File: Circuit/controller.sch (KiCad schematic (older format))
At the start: 13 parts, among them SW2 ROTARY_ENCODER_SWITCH, SW4 A, SW6 B, U4 JOYSTICK_W_BUTTON

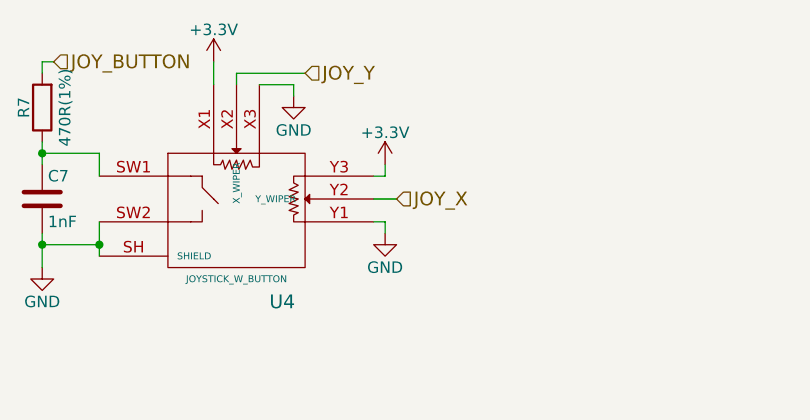
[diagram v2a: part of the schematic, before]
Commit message: Just caught I/O error on controller sch. XY reversed.
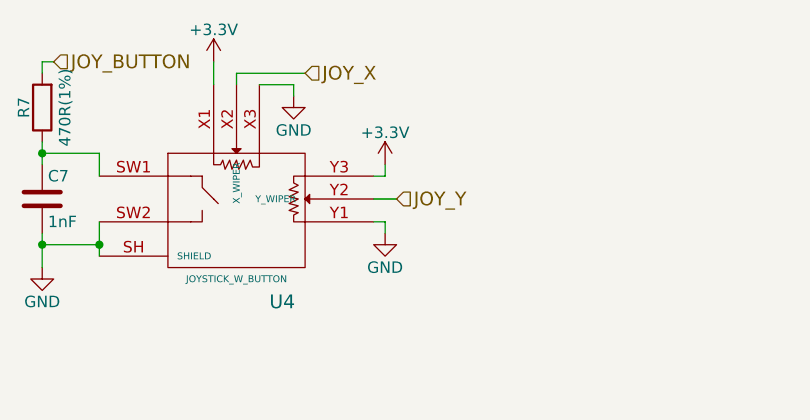
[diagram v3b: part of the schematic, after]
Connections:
- net JOY_X: now also U4.X2 (X_WIPER); no longer U4.Y2 (Y_WIPER)
- net JOY_Y: now also U4.Y2 (Y_WIPER); no longer U4.X2 (X_WIPER)
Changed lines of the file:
@@
 Text HLabel 1000 850  2    60   Input ~ 0
 JOY_BUTTON
+Text HLabel 2100 900  2    60   Input ~ 0
+JOY_X
 Text HLabel 2500 1450 2    60   Input ~ 0
-JOY_X
-Text HLabel 2100 900  2    60   Input ~ 0
 JOY_Y
 Wire Wire Line

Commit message: Modifications for BOM generation & documentation. LAST COMMIT WAS v0.1 PROTOTYPE.
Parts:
- SW2, SW4, SW6, U4: Non-Digikey (none) -> 1
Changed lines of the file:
@@
 F 2 "freetronics_footprints:JOYSTICK_W_BUTTON" H 1800 1450 60  0001 C CNN
 F 3 "" H 1900 850 60  0000 C CNN
+F 4 "1" H 1800 1450 60  0001 C CNN "Non-Digikey"
 	1    1800 1450
 	1    0    0    -1
@@
 F 2 "freetronics_footprints:SW_PUSHBUTTON_PTH" H 4950 1300 50  0001 C CNN
 F 3 "" H 4950 1300 50  0000 C CNN
+F 4 "1" H 4950 1300 60  0001 C CNN "Non-Digikey"
 	1    4950 1300
 	0    -1   -1   0
@@
 F 2 "freetronics_footprints:SW_PUSHBUTTON_PTH" H 4950 2350 50  0001 C CNN
 F 3 "" H 4950 2350 50  0000 C CNN
+F 4 "1" H 4950 2350 60  0001 C CNN "Non-Digikey"
 	1    4950 2350
 	0    -1   -1   0
@@
 F 2 "libs:EC11" H 2100 3910 50  0001 C CNN
 F 3 "" H 2200 4010 50  0001 C CNN
+F 4 "1" H 2200 3750 60  0001 C CNN "Non-Digikey"
 	1    2200 3750
 	1    0    0    -1

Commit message: pcb footprint updates
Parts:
- SW2: value ROTARY_ENCODER_SWITCH -> ROTARY_ENCODER
- U4: value JOYSTICK_W_BUTTON -> JOYSTICK
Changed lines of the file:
@@
 P 1800 1450
 F 0 "U4" H 2000 1000 60  0000 C CNN
-F 1 "JOYSTICK_W_BUTTON" H 1800 1100 30  0000 C CNN
+F 1 "JOYSTICK" H 1800 1100 30  0000 C CNN
 F 2 "freetronics_footprints:JOYSTICK_W_BUTTON" H 1800 1450 60  0001 C CNN
 F 3 "" H 1900 850 60  0000 C CNN
@@
 $EndComp
 $Comp
-L GND #PWR046
+L GND #PWR047
 U 1 1 58137F56
 P 950 1750
-F 0 "#PWR046" H 950 1500 50  0001 C CNN
+F 0 "#PWR047" H 950 1500 50  0001 C CNN
 F 1 "GND" H 950 1600 50  0000 C CNN
 F 2 "" H 950 1750 50  0000 C CNN
@@
 $EndComp
 $Comp
-L +3.3V #PWR047
+L +3.3V #PWR048
 U 1 1 58137F70
 P 1700 850
-F 0 "#PWR047" H 1700 700 50  0001 C CNN
+F 0 "#PWR048" H 1700 700 50  0001 C CNN
 F 1 "+3.3V" H 1700 990 50  0000 C CNN
 F 2 "" H 1700 850 50  0000 C CNN
@@
 	2050 950  2050 1000
 $Comp
-L GND #PWR048
+L GND #PWR049
 U 1 1 581380AB
 P 2050 1000
-F 0 "#PWR048" H 2050 750 50  0001 C CNN
+F 0 "#PWR049" H 2050 750 50  0001 C CNN
 F 1 "GND" H 2050 850 50  0000 C CNN
 F 2 "" H 2050 1000 50  0000 C CNN
@@
 	2450 1350 2450 1300
 $Comp
-L GND #PWR049
+L GND #PWR050
 U 1 1 58138157
 P 2450 1600
-F 0 "#PWR049" H 2450 1350 50  0001 C CNN
+F 0 "#PWR050" H 2450 1350 50  0001 C CNN
 F 1 "GND" H 2450 1450 50  0000 C CNN
 F 2 "" H 2450 1600 50  0000 C CNN
@@
 $EndComp
 $Comp
-L +3.3V #PWR050
+L +3.3V #PWR051
 U 1 1 5813816B
 P 2450 1300
-F 0 "#PWR050" H 2450 1150 50  0001 C CNN
+F 0 "#PWR051" H 2450 1150 50  0001 C CNN
 F 1 "+3.3V" H 2450 1440 50  0000 C CNN
 F 2 "" H 2450 1300 50  0000 C CNN
@@
 $EndComp
 $Comp
-L GND #PWR051
+L GND #PWR052
 U 1 1 5813C06B
 P 4950 1700
-F 0 "#PWR051" H 4950 1450 50  0001 C CNN
+F 0 "#PWR052" H 4950 1450 50  0001 C CNN
 F 1 "GND" H 4950 1550 50  0000 C CNN
 F 2 "" H 4950 1700 50  0000 C CNN
@@
 $EndComp
 $Comp
-L GND #PWR052
+L GND #PWR053
 U 1 1 5813C2E9
 P 4950 2750
-F 0 "#PWR052" H 4950 2500 50  0001 C CNN
+F 0 "#PWR053" H 4950 2500 50  0001 C CNN
 F 1 "GND" H 4950 2600 50  0000 C CNN
 F 2 "" H 4950 2750 50  0000 C CNN
@@
 P 2200 3750
 F 0 "SW2" H 2200 4010 50  0000 C CNN
-F 1 "ROTARY_ENCODER_SWITCH" H 2200 3490 50  0000 C CNN
+F 1 "ROTARY_ENCODER" H 2200 3490 50  0000 C CNN
 F 2 "libs:EC11" H 2100 3910 50  0001 C CNN
 F 3 "" H 2200 4010 50  0001 C CNN
@@
 $EndComp
 $Comp
-L GND #PWR053
+L GND #PWR054
 U 1 1 58141715
 P 1550 3950
-F 0 "#PWR053" H 1550 3700 50  0001 C CNN
+F 0 "#PWR054" H 1550 3700 50  0001 C CNN
 F 1 "GND" H 1550 3800 50  0000 C CNN
 F 2 "" H 1550 3950 50  0000 C CNN
@@
 	1550 3750 1900 3750
 $Comp
-L GND #PWR054
+L GND #PWR055
 U 1 1 58141924
 P 2800 3950
-F 0 "#PWR054" H 2800 3700 50  0001 C CNN
+F 0 "#PWR055" H 2800 3700 50  0001 C CNN
 F 1 "GND" H 2800 3800 50  0000 C CNN
 F 2 "" H 2800 3950 50  0000 C CNN
@@
 	2800 3850 2500 3850
 $Comp
-L +3.3V #PWR055
+L +3.3V #PWR056
 U 1 1 58141A8C
 P 3000 3550
-F 0 "#PWR055" H 3000 3400 50  0001 C CNN
+F 0 "#PWR056" H 3000 3400 50  0001 C CNN
 F 1 "+3.3V" H 3000 3690 50  0000 C CNN
 F 2 "" H 3000 3550 50  0000 C CNN
@@
 	2550 3300 2550 3650
 $Comp
-L +3.3V #PWR056
+L +3.3V #PWR057
 U 1 1 58141FF1
 P 1250 3100
-F 0 "#PWR056" H 1250 2950 50  0001 C CNN
+F 0 "#PWR057" H 1250 2950 50  0001 C CNN
 F 1 "+3.3V" H 1250 3240 50  0000 C CNN
 F 2 "" H 1250 3100 50  0000 C CNN

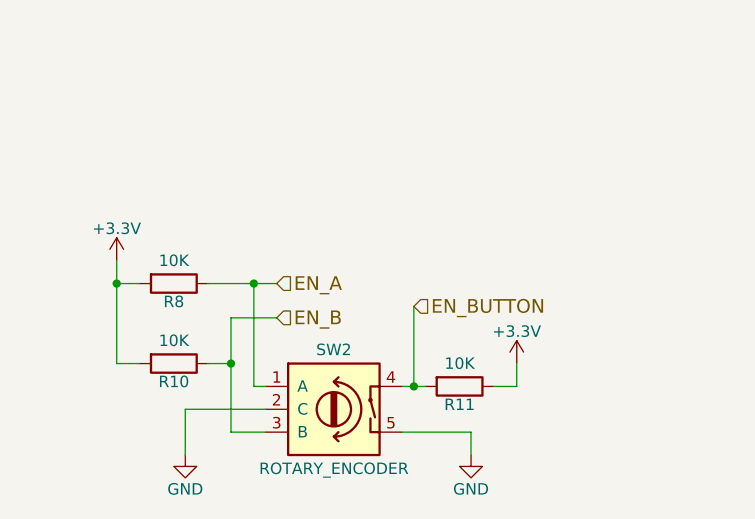
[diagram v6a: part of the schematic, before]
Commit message: Added 10k resistors on pins from quadrature out on encoder. Fixes #16.
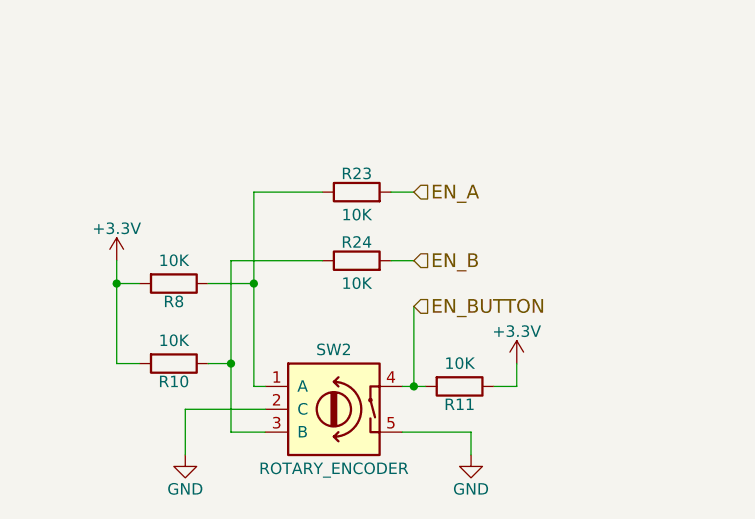
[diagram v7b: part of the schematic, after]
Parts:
- added R23, R24: 10K, Resistors_SMD:R_0603_HandSoldering, symbol R
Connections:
- net EN_A: now also R23.2; no longer R8.1, SW2.1 (A)
- net EN_B: now also R24.2; no longer R10.1, SW2.3 (B)
- new net: R23.1, R8.1, SW2.1 (A)
- new net: R10.1, R24.1, SW2.3 (B)
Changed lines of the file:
@@
 $EndComp
 $Comp
-L GND #PWR047
+L GND #PWR43
 U 1 1 58137F56
 P 950 1750
-F 0 "#PWR047" H 950 1500 50  0001 C CNN
+F 0 "#PWR43" H 950 1500 50  0001 C CNN
 F 1 "GND" H 950 1600 50  0000 C CNN
 F 2 "" H 950 1750 50  0000 C CNN
@@
 $EndComp
 $Comp
-L +3.3V #PWR048
+L +3.3V #PWR46
 U 1 1 58137F70
 P 1700 850
-F 0 "#PWR048" H 1700 700 50  0001 C CNN
+F 0 "#PWR46" H 1700 700 50  0001 C CNN
 F 1 "+3.3V" H 1700 990 50  0000 C CNN
 F 2 "" H 1700 850 50  0000 C CNN
@@
 	1    0    0    -1
 $EndComp
-Wire Wire Line
-	1200 1550 1200 1700
-Wire Wire Line
-	1200 1650 950  1650
-Wire Wire Line
-	950  1600 950  1750
-Connection ~ 1200 1650
-Connection ~ 950  1650
-Wire Wire Line
-	1200 1350 1200 1250
-Wire Wire Line
-	1200 1250 950  1250
-Wire Wire Line
-	950  1200 950  1300
-Connection ~ 950  1250
-Wire Wire Line
-	950  900  950  850
-Wire Wire Line
-	1900 950  2050 950
-Wire Wire Line
-	2050 950  2050 1000
-$Comp
-L GND #PWR049
+$Comp
+L GND #PWR47
 U 1 1 581380AB
 P 2050 1000
-F 0 "#PWR049" H 2050 750 50  0001 C CNN
+F 0 "#PWR47" H 2050 750 50  0001 C CNN
 F 1 "GND" H 2050 850 50  0000 C CNN
 F 2 "" H 2050 1000 50  0000 C CNN
@@
 	1    0    0    -1
 $EndComp
-Wire Wire Line
-	1800 950  1800 900
-Wire Wire Line
-	1800 900  2100 900
-Wire Wire Line
-	1700 950  1700 850
-Wire Wire Line
-	2400 1550 2450 1550
-Wire Wire Line
-	2450 1550 2450 1600
-Wire Wire Line
-	2400 1350 2450 1350
-Wire Wire Line
-	2450 1350 2450 1300
-$Comp
-L GND #PWR050
+$Comp
+L GND #PWR49
 U 1 1 58138157
 P 2450 1600
-F 0 "#PWR050" H 2450 1350 50  0001 C CNN
+F 0 "#PWR49" H 2450 1350 50  0001 C CNN
 F 1 "GND" H 2450 1450 50  0000 C CNN
 F 2 "" H 2450 1600 50  0000 C CNN
@@
 $EndComp
 $Comp
-L +3.3V #PWR051
+L +3.3V #PWR48
 U 1 1 5813816B
 P 2450 1300
-F 0 "#PWR051" H 2450 1150 50  0001 C CNN
+F 0 "#PWR48" H 2450 1150 50  0001 C CNN
 F 1 "+3.3V" H 2450 1440 50  0000 C CNN
 F 2 "" H 2450 1300 50  0000 C CNN
@@
 	1    0    0    -1
 $EndComp
-Wire Wire Line
-	2400 1450 2500 1450
 Text HLabel 1000 850  2    60   Input ~ 0
 JOY_BUTTON
@@
 Text HLabel 2500 1450 2    60   Input ~ 0
 JOY_Y
-Wire Wire Line
-	950  850  1000 850
 $Comp
 L SW_PUSH SW4
@@
 $EndComp
 $Comp
-L GND #PWR052
+L GND #PWR52
 U 1 1 5813C06B
 P 4950 1700
-F 0 "#PWR052" H 4950 1450 50  0001 C CNN
+F 0 "#PWR52" H 4950 1450 50  0001 C CNN
 F 1 "GND" H 4950 1550 50  0000 C CNN
 F 2 "" H 4950 1700 50  0000 C CNN
@@
 	1    0    0    -1
 $EndComp
-Wire Wire Line
-	4950 1600 4950 1700
-Wire Wire Line
-	4950 1650 5200 1650
-Wire Wire Line
-	5200 1650 5200 1450
-Connection ~ 4950 1650
-Wire Wire Line
-	4950 1000 5300 1000
-Wire Wire Line
-	5200 1150 5200 1000
-Connection ~ 5200 1000
 $Comp
 L SW_PUSH SW6
@@
 $EndComp
 $Comp
-L GND #PWR053
+L GND #PWR53
 U 1 1 5813C2E9
 P 4950 2750
-F 0 "#PWR053" H 4950 2500 50  0001 C CNN
+F 0 "#PWR53" H 4950 2500 50  0001 C CNN
 F 1 "GND" H 4950 2600 50  0000 C CNN
 F 2 "" H 4950 2750 50  0000 C CNN
@@
 	1    0    0    -1
 $EndComp
-Wire Wire Line
-	4950 2650 4950 2750
-Wire Wire Line
-	4950 2700 5200 2700
-Wire Wire Line
-	5200 2700 5200 2500
-Connection ~ 4950 2700
-Wire Wire Line
-	4950 2050 5300 2050
-Wire Wire Line
-	5200 2200 5200 2050
-Connection ~ 5200 2050
-Wire Wire Line
-	5600 1000 5700 1000
-Wire Wire Line
-	5600 2050 5700 2050
 Text HLabel 5700 1000 2    60   Input ~ 0
 A_BUTTON
@@
 $EndComp
 $Comp
-L GND #PWR054
+L GND #PWR45
 U 1 1 58141715
 P 1550 3950
-F 0 "#PWR054" H 1550 3700 50  0001 C CNN
+F 0 "#PWR45" H 1550 3700 50  0001 C CNN
 F 1 "GND" H 1550 3800 50  0000 C CNN
 F 2 "" H 1550 3950 50  0000 C CNN
@@
 	1    0    0    -1
 $EndComp
-Wire Wire Line
-	1550 3950 1550 3750
-Wire Wire Line
-	1550 3750 1900 3750
-$Comp
-L GND #PWR055
+$Comp
+L GND #PWR50
 U 1 1 58141924
 P 2800 3950
-F 0 "#PWR055" H 2800 3700 50  0001 C CNN
+F 0 "#PWR50" H 2800 3700 50  0001 C CNN
 F 1 "GND" H 2800 3800 50  0000 C CNN
 F 2 "" H 2800 3950 50  0000 C CNN
@@
 	1    0    0    -1
 $EndComp
-Wire Wire Line
-	2800 3950 2800 3850
-Wire Wire Line
-	2800 3850 2500 3850
-$Comp
-L +3.3V #PWR056
+$Comp
+L +3.3V #PWR51
 U 1 1 58141A8C
 P 3000 3550
-F 0 "#PWR056" H 3000 3400 50  0001 C CNN
+F 0 "#PWR51" H 3000 3400 50  0001 C CNN
 F 1 "+3.3V" H 3000 3690 50  0000 C CNN
 F 2 "" H 3000 3550 50  0000 C CNN
@@
 	1    0    0    -1
 $EndComp
-Wire Wire Line
-	2900 3650 3000 3650
-Wire Wire Line
-	3000 3650 3000 3550
-Wire Wire Line
-	2500 3650 2600 3650
-Connection ~ 2550 3650
 Text HLabel 2550 3300 2    60   Input ~ 0
 EN_BUTTON
-Wire Wire Line
-	2550 3300 2550 3650
-$Comp
-L +3.3V #PWR057
+$Comp
+L +3.3V #PWR44
 U 1 1 58141FF1
 P 1250 3100
-F 0 "#PWR057" H 1250 2950 50  0001 C CNN
+F 0 "#PWR44" H 1250 2950 50  0001 C CNN
 F 1 "+3.3V" H 1250 3240 50  0000 C CNN
 F 2 "" H 1250 3100 50  0000 C CNN
@@
 	1    0    0    -1
 $EndComp
-Wire Wire Line
-	1250 3100 1250 3550
-Wire Wire Line
-	1250 3550 1350 3550
-Wire Wire Line
-	1350 3200 1250 3200
-Connection ~ 1250 3200
-Wire Wire Line
-	1900 3650 1850 3650
-Wire Wire Line
-	1850 3650 1850 3200
-Wire Wire Line
-	1650 3200 1950 3200
-Wire Wire Line
-	1750 3850 1900 3850
-Wire Wire Line
-	1750 3350 1750 3850
-Wire Wire Line
-	1750 3550 1650 3550
-Text HLabel 1950 3200 2    60   Input ~ 0
+Text HLabel 2550 2800 2    60   Input ~ 0
 EN_A
-Text HLabel 1950 3350 2    60   Input ~ 0
+Text HLabel 2550 3100 2    60   Input ~ 0
 EN_B
-Wire Wire Line
-	1950 3350 1750 3350
-Connection ~ 1750 3550
-Connection ~ 1850 3200
 $Comp
 L R R8
@@
 	1    0    0    -1
 $EndComp
+$Comp
+L R R23
+U 1 1 584686C9
+P 2300 2800
+F 0 "R23" V 2380 2800 50  0000 C CNN
+F 1 "10K" V 2200 2800 50  0000 C CNN
+F 2 "Resistors_SMD:R_0603_HandSoldering" V 2230 2800 50  0001 C CNN
+F 3 "" H 2300 2800 50  0000 C CNN
+F 4 "311-10KGRCT-ND" V 2300 2800 60  0001 C CNN "Digikey PN"
+F 5 "http://www.digikey.com.au/product-detail/en/yageo/RC0603JR-0710KL/311-10KGRCT-ND/729647" V 2300 2800 60  0001 C CNN "Link"
+F 6 "RC0603JR-0710KL" V 2300 2800 60  0001 C CNN "Manufacturer PN"
+F 7 "0.10" V 2300 2800 60  0001 C CNN "Unit Cost"
+	1    2300 2800
+	0    -1   -1   0
+$EndComp
+$Comp
+L R R24
+U 1 1 5846876B
+P 2300 3100
+F 0 "R24" V 2380 3100 50  0000 C CNN
+F 1 "10K" V 2200 3100 50  0000 C CNN
+F 2 "Resistors_SMD:R_0603_HandSoldering" V 2230 3100 50  0001 C CNN
+F 3 "" H 2300 3100 50  0000 C CNN
+F 4 "311-10KGRCT-ND" V 2300 3100 60  0001 C CNN "Digikey PN"
+F 5 "http://www.digikey.com.au/product-detail/en/yageo/RC0603JR-0710KL/311-10KGRCT-ND/729647" V 2300 3100 60  0001 C CNN "Link"
+F 6 "RC0603JR-0710KL" V 2300 3100 60  0001 C CNN "Manufacturer PN"
+F 7 "0.10" V 2300 3100 60  0001 C CNN "Unit Cost"
+	1    2300 3100
+	0    -1   -1   0
+$EndComp
+Wire Wire Line
+	1200 1550 1200 1700
+Wire Wire Line
+	1200 1650 950  1650
+Wire Wire Line
+	950  1600 950  1750
+Connection ~ 1200 1650
+Connection ~ 950  1650
+Wire Wire Line
+	1200 1350 1200 1250
+Wire Wire Line
+	1200 1250 950  1250
+Wire Wire Line
+	950  1200 950  1300
+Connection ~ 950  1250
+Wire Wire Line
+	950  900  950  850
+Wire Wire Line
+	1900 950  2050 950
+Wire Wire Line
+	2050 950  2050 1000
+Wire Wire Line
+	1800 950  1800 900
+Wire Wire Line
+	1800 900  2100 900
+Wire Wire Line
+	1700 950  1700 850
+Wire Wire Line
+	2400 1550 2450 1550
+Wire Wire Line
+	2450 1550 2450 1600
+Wire Wire Line
+	2400 1350 2450 1350
+Wire Wire Line
+	2450 1350 2450 1300
+Wire Wire Line
+	2400 1450 2500 1450
+Wire Wire Line
+	950  850  1000 850
+Wire Wire Line
+	4950 1600 4950 1700
+Wire Wire Line
+	4950 1650 5200 1650
+Wire Wire Line
+	5200 1650 5200 1450
+Connection ~ 4950 1650
+Wire Wire Line
+	4950 1000 5300 1000
+Wire Wire Line
+	5200 1150 5200 1000
+Connection ~ 5200 1000
+Wire Wire Line
+	4950 2650 4950 2750
+Wire Wire Line
+	4950 2700 5200 2700
+Wire Wire Line
+	5200 2700 5200 2500
+Connection ~ 4950 2700
+Wire Wire Line
+	4950 2050 5300 2050
+Wire Wire Line
+	5200 2200 5200 2050
+Connection ~ 5200 2050
+Wire Wire Line
+	5600 1000 5700 1000
+Wire Wire Line
+	5600 2050 5700 2050
+Wire Wire Line
+	1550 3950 1550 3750
+Wire Wire Line
+	1550 3750 1900 3750
+Wire Wire Line
+	2800 3950 2800 3850
+Wire Wire Line
+	2800 3850 2500 3850
+Wire Wire Line
+	2900 3650 3000 3650
+Wire Wire Line
+	3000 3650 3000 3550
+Wire Wire Line
+	2500 3650 2600 3650
+Connection ~ 2550 3650
+Wire Wire Line
+	2550 3300 2550 3650
+Wire Wire Line
+	1250 3100 1250 3550
+Wire Wire Line
+	1250 3550 1350 3550
+Wire Wire Line
+	1350 3200 1250 3200
+Connection ~ 1250 3200
+Wire Wire Line
+	1850 3650 1900 3650
+Wire Wire Line
+	1850 2800 1850 3650
+Wire Wire Line
+	1850 3200 1650 3200
+Wire Wire Line
+	1750 3850 1900 3850
+Wire Wire Line
+	1750 3100 1750 3850
+Wire Wire Line
+	1750 3550 1650 3550
+Connection ~ 1750 3550
+Connection ~ 1850 3200
+Wire Wire Line
+	1850 2800 2150 2800
+Wire Wire Line
+	2150 3100 1750 3100
+Wire Wire Line
+	2450 3100 2550 3100
+Wire Wire Line
+	2450 2800 2550 2800
 $EndSCHEMATC

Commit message: BOM changes to fix #15, fix #24.
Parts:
- C7, C8, C9: Digikey PN 490-3184-1-ND -> 490-1494-1-ND; Link http://www.digikey.com.au/product-detail/en/murata-electron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 -> http://www.digikey.com/product-detail/en/murata-electronics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; Manufacturer PN GRM033R71E102KA01D -> GRM188R71H102KA01D
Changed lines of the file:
@@
-$EndComp
-$Comp
-L C C8
-U 1 1 5813BFC7
-P 5200 1300
-F 0 "C8" H 5225 1400 50  0000 L CNN
-F 1 "1nF" H 5225 1200 50  0000 L CNN
-F 2 "Capacitors_SMD:C_0603_HandSoldering" H 5238 1150 50  0001 C CNN
-F 3 "" H 5200 1300 50  0000 C CNN
-F 4 "490-3184-1-ND" H 5200 1300 60  0001 C CNN "Digikey PN"
-F 5 "http://www.digikey.com.au/product-detail/en/murata-electronics-north-america/GRM033R71E102KA01D/490-3184-1-ND/702725" H 5200 1300 60  0001 C CNN "Link"
-F 6 "GRM033R71E102KA01D" H 5200 1300 60  0001 C CNN "Manufacturer PN"
-F 7 "0.10" H 5200 1300 60  0001 C CNN "Unit Cost"
-	1    5200 1300
-	1    0    0    -1
 $EndComp
 $Comp
@@
 $EndComp
 $Comp
-L C C9
-U 1 1 58230857
-P 5200 2350
-F 0 "C9" H 5225 2450 50  0000 L CNN
-F 1 "1nF" H 5225 2250 50  0000 L CNN
-F 2 "Capacitors_SMD:C_0603_HandSoldering" H 5238 2200 50  0001 C CNN
-F 3 "" H 5200 2350 50  0000 C CNN
-F 4 "490-3184-1-ND" H 5200 2350 60  0001 C CNN "Digikey PN"
-F 5 "http://www.digikey.com.au/product-detail/en/murata-electronics-north-america/GRM033R71E102KA01D/490-3184-1-ND/702725" H 5200 2350 60  0001 C CNN "Link"
-F 6 "GRM033R71E102KA01D" H 5200 2350 60  0001 C CNN "Manufacturer PN"
-F 7 "0.10" H 5200 2350 60  0001 C CNN "Unit Cost"
-	1    5200 2350
-	1    0    0    -1
-$EndComp
-$Comp
 L C C7
 U 1 1 582308E6
@@
 F 2 "Capacitors_SMD:C_0603_HandSoldering" H 988 1300 50  0001 C CNN
 F 3 "" H 950 1450 50  0000 C CNN
-F 4 "490-3184-1-ND" H 950 1450 60  0001 C CNN "Digikey PN"
-F 5 "http://www.digikey.com.au/product-detail/en/murata-electronics-north-america/GRM033R71E102KA01D/490-3184-1-ND/702725" H 950 1450 60  0001 C CNN "Link"
-F 6 "GRM033R71E102KA01D" H 950 1450 60  0001 C CNN "Manufacturer PN"
+F 4 "490-1494-1-ND" H 950 1450 60  0001 C CNN "Digikey PN"
+F 5 "http://www.digikey.com/product-detail/en/murata-electronics-north-america/GRM188R71H102KA01D/490-1494-1-ND/587851" H 950 1450 60  0001 C CNN "Link"
+F 6 "GRM188R71H102KA01D" H 950 1450 60  0001 C CNN "Manufacturer PN"
 F 7 "0.10" H 950 1450 60  0001 C CNN "Unit Cost"
 	1    950  1450
@@
 Wire Wire Line
 	2450 2800 2550 2800
+$Comp
+L C C9
+U 1 1 5846C84A
+P 5200 2350
+F 0 "C9" H 5225 2450 50  0000 L CNN
+F 1 "1nF" H 5225 2250 50  0000 L CNN
+F 2 "Capacitors_SMD:C_0603_HandSoldering" H 5238 2200 50  0001 C CNN
+F 3 "" H 5200 2350 50  0000 C CNN
+F 4 "490-1494-1-ND" H 5200 2350 60  0001 C CNN "Digikey PN"
+F 5 "http://www.digikey.com/product-detail/en/murata-electronics-north-america/GRM188R71H102KA01D/490-1494-1-ND/587851" H 5200 2350 60  0001 C CNN "Link"
+F 6 "GRM188R71H102KA01D" H 5200 2350 60  0001 C CNN "Manufacturer PN"
+F 7 "0.10" H 5200 2350 60  0001 C CNN "Unit Cost"
+	1    5200 2350
+	1    0    0    -1
+$EndComp
+$Comp
+L C C8
+U 1 1 5846C7EA
+P 5200 1300
+F 0 "C8" H 5225 1400 50  0000 L CNN
+F 1 "1nF" H 5225 1200 50  0000 L CNN
+F 2 "Capacitors_SMD:C_0603_HandSoldering" H 5238 1150 50  0001 C CNN
+F 3 "" H 5200 1300 50  0000 C CNN
+F 4 "490-1494-1-ND" H 5200 1300 60  0001 C CNN "Digikey PN"
+F 5 "http://www.digikey.com/product-detail/en/murata-electronics-north-america/GRM188R71H102KA01D/490-1494-1-ND/587851" H 5200 1300 60  0001 C CNN "Link"
+F 6 "GRM188R71H102KA01D" H 5200 1300 60  0001 C CNN "Manufacturer PN"
+F 7 "0.10" H 5200 1300 60  0001 C CNN "Unit Cost"
+	1    5200 1300
+	1    0    0    -1
+$EndComp
 $EndSCHEMATC
